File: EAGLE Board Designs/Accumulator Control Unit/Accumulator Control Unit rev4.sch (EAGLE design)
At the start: 240 parts, among them J1 CONNECTOR-2_MF_T_V_, J100 CONNECTOR-8_S_S, J2 CONNECTOR-8_MF_T_V_, J3 CONNECTOR-14_MF_T_V_, J4 JUMPER__1X02, J5 CONNECTOR-12_MF_T_V_, J6 CONNECTOR-CAN_μF_S_RA_, J7 CONNECTOR-2_MOLEX_NANOFIT_PTH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, Q1 TRANSISTOR_N_MOS__PMV15ENEA, Q100 TRANSISTOR_N_MOS__PMV15ENEA, Q101 TRANSISTOR_N_MOS__PMV15ENEA, Q2 TRANSISTOR_N_MOS__PMV15ENEA, T1 TRANSFORMER_HM2112ZNLT_AIRGAP, U1 RELAY_SOLIDSTATE_NO_DIP-4, U10 MAX7404, U100 ADG1423, U101 LM555, U11 OPAMP_1_CHANNEL_OPA991, U12 LOGICGATE_AND_DCK3, U13 OPAMP_1_CHANNEL_OPA991, U14 LOGICGATE_AND_DCK3, U15 OPAMP_1_CHANNEL_OPA991, U16 LOGICGATE_AND_DCK3, U17 OPAMP_1_CHANNEL_OPA991, U18 OPAMP_1_CHANNEL_OPA991, U19 MAX7404, U2 RELAY_SOLIDSTATE_NO_DIP-4, U20 OPAMP_1_CHANNEL_OPA991, U21 OPAMP_1_CHANNEL_OPA991, U22 OPAMP_1_CHANNEL_OPA991, U23 OPAMP_1_CHANNEL_OPA991, U24 OPAMP_1_CHANNEL_OPA991, U25 MAX7404, U26 VOLTAGE_REGULATOR_SOT-223_3.3V, U27 TCAN1051HQV-Q1, U28 OPAMP_1_CHANNEL_OPA991, U29 TCAN1051HQV-Q1, U3 OPAMP_1_CHANNEL_OPA991, U4 MAX7404, U5 LTC6820, U6 LOGICGATE_BUFFER, U7 ADM8316WBX30, U8 RELAY_SOLIDSTATE_NO_DIP-4, U9 OPAMP_1_CHANNEL_OPA991

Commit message: minor tweaks
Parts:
- added C46: CAPACITOR_0603_10V_0.1UF, HyTechDevices:CAPACITOR_0603_10V_0.1UF
- added J8: JUMPER__1X02, HyTechDevices:JUMPER__1X02
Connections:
- new net N$35: J8.2, R91.2
- net +3V3: now also C46.2, U29.VIO
- net CANH: no longer J6.CANH
- net CANL: no longer J6.CANL
- net EM_CANH: now also J6.CANH, J8.1, U29.CANH; no longer J3.3
- net EM_CANL: now also J6.CANL, R89.2, U29.CANL; no longer J3.2
- net GND: now also C46.1, U29.S
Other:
- moved on the sheet: C45, R26, R27, R89, R91

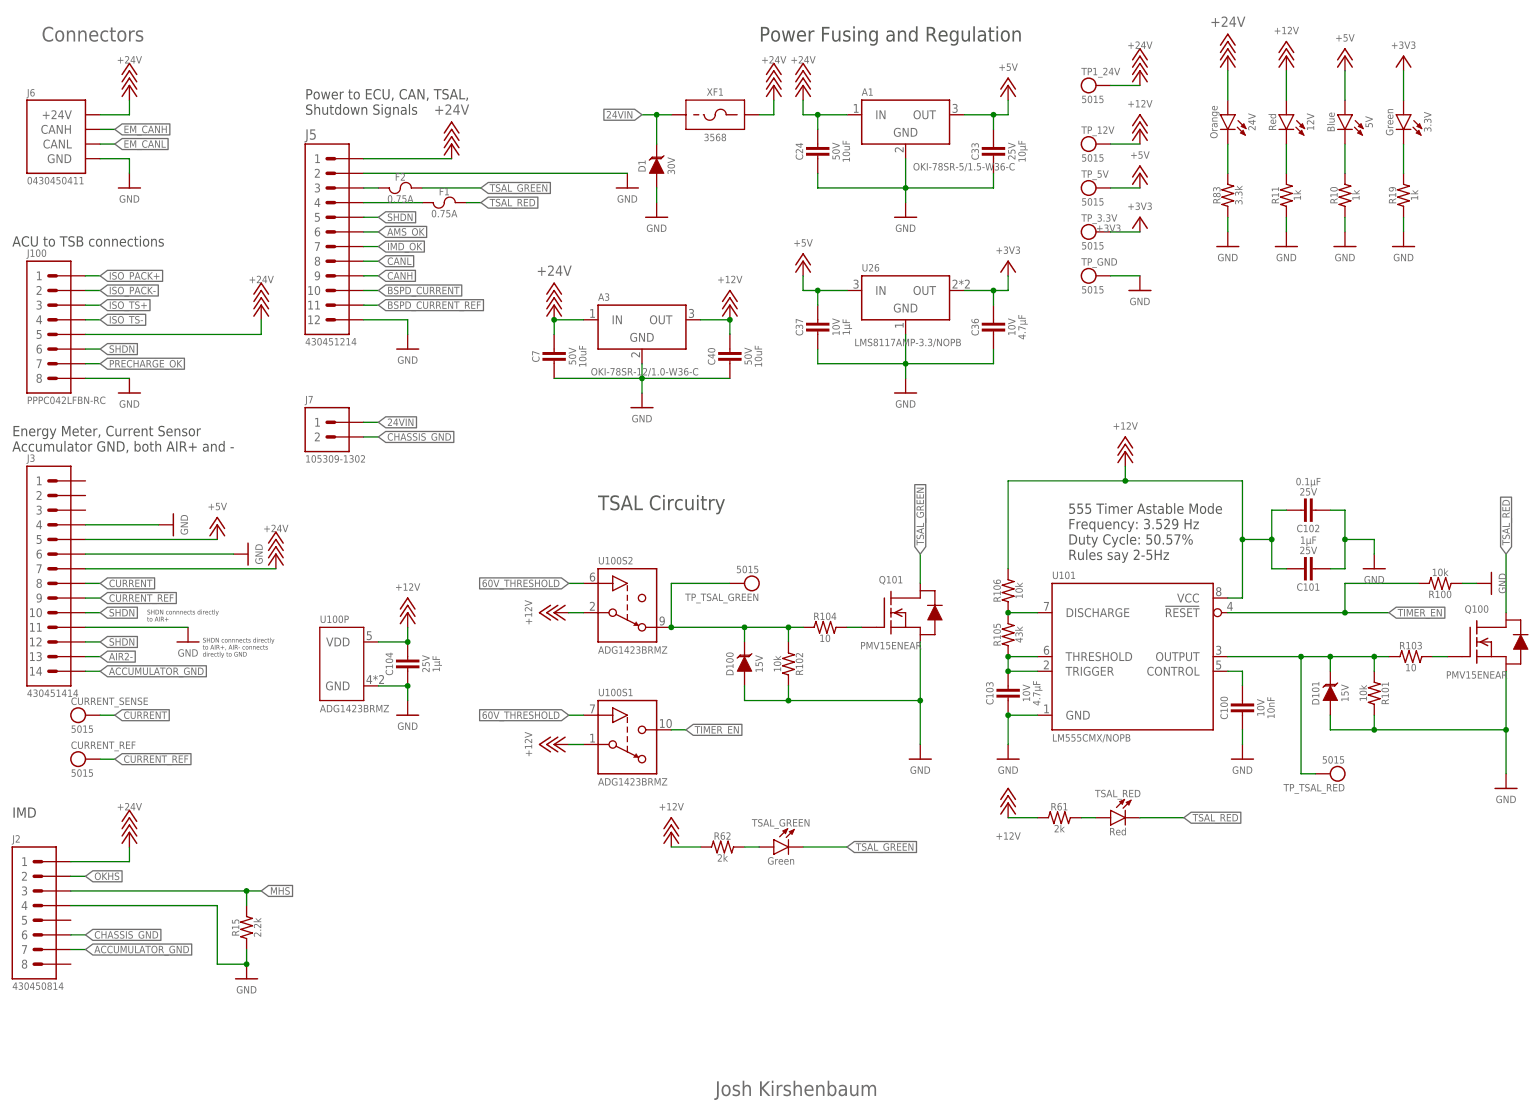
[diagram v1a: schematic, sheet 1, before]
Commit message: added inverter 24v switching
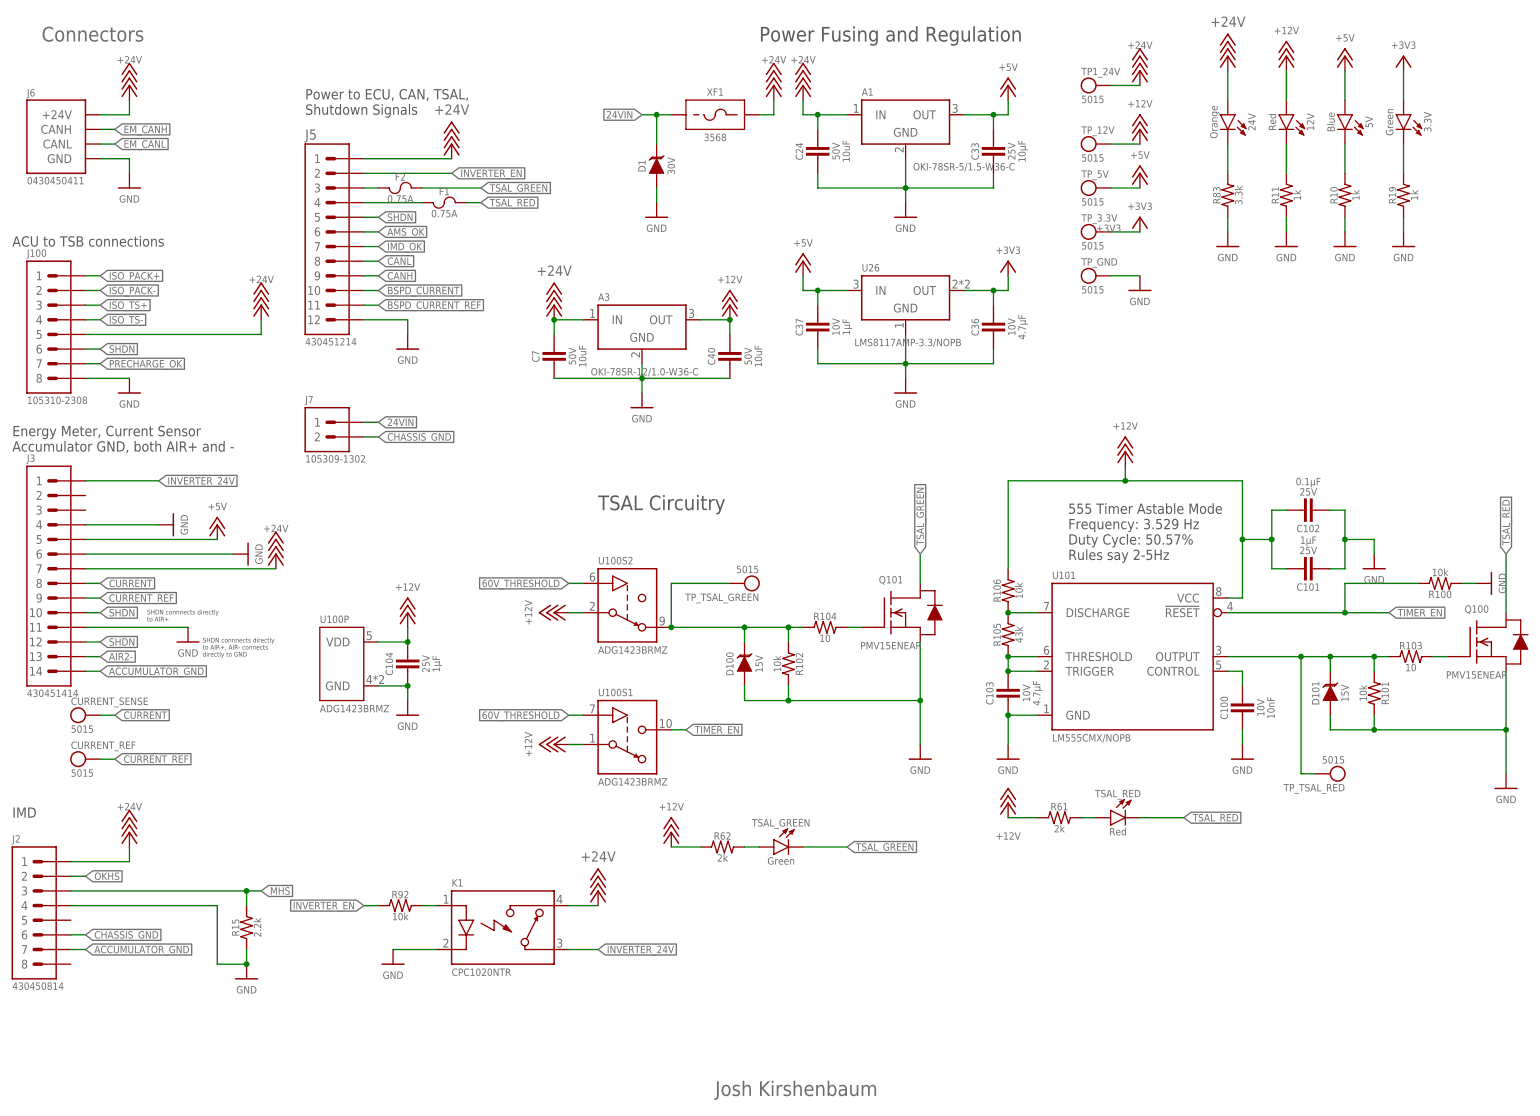
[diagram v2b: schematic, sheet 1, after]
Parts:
- added K1: RELAY_SOLIDSTATE_NO_CPC1020NTR, HyTechDevices:RELAY_SOLIDSTATE_NO_CPC1020NTR
- added R92: RESISTOR_0603_10K, HyTechDevices:RESISTOR_0603_10K
- J100: value CONNECTOR-8_S_S -> CONNECTOR-8_NF_T_V_NATURAL; device HyTechDevices:CONNECTOR-8_S_S -> HyTechDevices:CONNECTOR-8_NF_T_V_NATURAL
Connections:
- new net INVERTER_24V: J3.1, K1.CONTACT1
- new net INVERTER_EN: J5.2, R92.1
- new net N$38: K1.CONTROL+, R92.2
- net +24V: now also K1.CONTACT2
- net GND: now also K1.CONTROL-; no longer J5.2
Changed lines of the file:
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@@
 <part name="FRAME2" library="HyTechFrames" deviceset="FRAME" device=""/>
 <part name="FRAME4" library="HyTechFrames" deviceset="FRAME" device=""/>
-<part name="J100" library="HyTechDevices" deviceset="CONNECTOR-8_?_*" device="S" technology="S"/>
+<part name="J100" library="HyTechDevices" deviceset="CONNECTOR-8_?_*" device="NF_T_V" technology="NATURAL" value="CONNECTOR-8_NF_T_V_NATURAL"/>
 <part name="P1" library="HyTechSupplies" deviceset="+24V" device=""/>
 <part name="P2" library="HyTechSupplies" deviceset="GND" device=""/>
 <part name="P6" library="HyTechSupplies" deviceset="+24V" device=""/>
-<part name="P11" library="HyTechSupplies" deviceset="GND" device=""/>
 <part name="C24" library="HyTechDevices" deviceset="CAPACITOR_?_*" device="0805" technology="50V_10UF" value="CAPACITOR_0805_50V_10UF"/>
 <part name="C33" library="HyTechDevices" deviceset="CAPACITOR_?_*" device="0603" technology="25V_10UF"/>
@@
 <part name="P121" library="HyTechSupplies" deviceset="GND" device=""/>
 <part name="P122" library="HyTechSupplies" deviceset="GND" device=""/>
+<part name="K1" library="HyTechDevices" deviceset="RELAY_SOLIDSTATE_NO_*" device="CPC1020NTR"/>
+<part name="U$30" library="HyTechSupplies" deviceset="+24V" device=""/>
+<part name="P11" library="HyTechSupplies" deviceset="GND" device=""/>
+<part name="R92" library="HyTechDevices" deviceset="RESISTOR_?_*" device="0603" technology="10K"/>
 </parts>
 <sheets>
@@
 <attribute name="VALUE" x="50.8" y="163.83" size="1.27" layer="96" align="bottom-center"/>
 </instance>
-<instance part="P11" gate="1" x="114.3" y="180.34" smashed="yes">
-<attribute name="VALUE" x="114.3" y="179.07" size="1.27" layer="96" align="top-center"/>
-</instance>
 <instance part="C24" gate="G$1" x="147.32" y="187.96" smashed="yes" rot="R90">
 <attribute name="NAME" x="144.78" y="186.69" size="1.27" layer="95" rot="R90" align="bottom-center"/>
@@
 <instance part="P115" gate="1" x="76.2" y="152.4" smashed="yes">
 <attribute name="VALUE" x="76.2" y="151.13" size="1.27" layer="96" align="top-center"/>
+</instance>
+<instance part="K1" gate="G$1" x="83.82" y="58.42" smashed="yes">
+<attribute name="NAME" x="83.82" y="59.182" size="1.27" layer="95"/>
+<attribute name="MPN" x="83.82" y="44.958" size="1.27" layer="96" align="top-left"/>
+</instance>
+<instance part="U$30" gate="G$1" x="109.22" y="58.42" smashed="yes">
+<attribute name="VALUE" x="109.22" y="63.5" size="1.778" layer="96" align="bottom-center"/>
+</instance>
+<instance part="P11" gate="1" x="73.66" y="45.72" smashed="yes">
+<attribute name="VALUE" x="73.66" y="44.45" size="1.27" layer="96" align="top-center"/>
+</instance>
+<instance part="R92" gate="G$1" x="76.2" y="55.88" smashed="yes">
+<attribute name="NAME" x="74.93" y="57.15" size="1.27" layer="95" align="bottom-center"/>
+<attribute name="RESISTANCE" x="74.93" y="54.61" size="1.27" layer="96" align="top-center"/>
 </instance>
 </instances>
@@
 <wire x1="27.94" y1="185.42" x2="27.94" y2="182.88" width="0.1524" layer="91"/>
 <pinref part="J6" gate="G$1" pin="GND"/>
-</segment>
-<segment>
-<wire x1="68.58" y1="182.88" x2="114.3" y2="182.88" width="0.1524" layer="91"/>
-<pinref part="P11" gate="1" pin="GND"/>
-<pinref part="J5" gate="G$1" pin="2"/>
 </segment>
 <segment>
@@
 <wire x1="68.58" y1="157.48" x2="76.2" y2="157.48" width="0.1524" layer="91"/>
 <wire x1="76.2" y1="157.48" x2="76.2" y2="154.94" width="0.1524" layer="91"/>
+</segment>
+<segment>
+<pinref part="K1" gate="G$1" pin="CONTROL-"/>
+<wire x1="81.28" y1="48.26" x2="73.66" y2="48.26" width="0.1524" layer="91"/>
+<pinref part="P11" gate="1" pin="GND"/>
 </segment>
 </net>
@@
 <wire x1="68.58" y1="185.42" x2="83.82" y2="185.42" width="0.1524" layer="91"/>
 </segment>
+<segment>
+<pinref part="U$30" gate="G$1" pin="+24V"/>
+<pinref part="K1" gate="G$1" pin="CONTACT2"/>
+<wire x1="109.22" y1="55.88" x2="104.14" y2="55.88" width="0.1524" layer="91"/>
+</segment>
 </net>
 <net name="N$32" class="0">
@@
 </segment>
 </net>
+<net name="INVERTER_EN" class="0">
+<segment>
+<pinref part="J5" gate="G$1" pin="2"/>
+<wire x1="68.58" y1="182.88" x2="83.82" y2="182.88" width="0.1524" layer="91"/>
+<label x="83.82" y="182.88" size="1.27" layer="95" xref="yes"/>
+</segment>
+<segment>
+<wire x1="68.58" y1="55.88" x2="71.12" y2="55.88" width="0.1524" layer="91"/>
+<label x="68.58" y="55.88" size="1.27" layer="95" rot="R180" xref="yes"/>
+<pinref part="R92" gate="G$1" pin="1"/>
+</segment>
+</net>
+<net name="INVERTER_24V" class="0">
+<segment>
+<pinref part="J3" gate="G$1" pin="1"/>
+<wire x1="20.32" y1="129.54" x2="33.02" y2="129.54" width="0.1524" layer="91"/>
+<label x="33.02" y="129.54" size="1.27" layer="95" xref="yes"/>
+</segment>
+<segment>
+<pinref part="K1" gate="G$1" pin="CONTACT1"/>
+<wire x1="104.14" y1="48.26" x2="109.22" y2="48.26" width="0.1524" layer="91"/>
+<label x="109.22" y="48.26" size="1.27" layer="95" xref="yes"/>
+</segment>
+</net>
+<net name="N$38" class="0">
+<segment>
+<pinref part="K1" gate="G$1" pin="CONTROL+"/>
+<wire x1="81.28" y1="55.88" x2="78.74" y2="55.88" width="0.1524" layer="91"/>
+<pinref part="R92" gate="G$1" pin="2"/>
+</segment>
+</net>

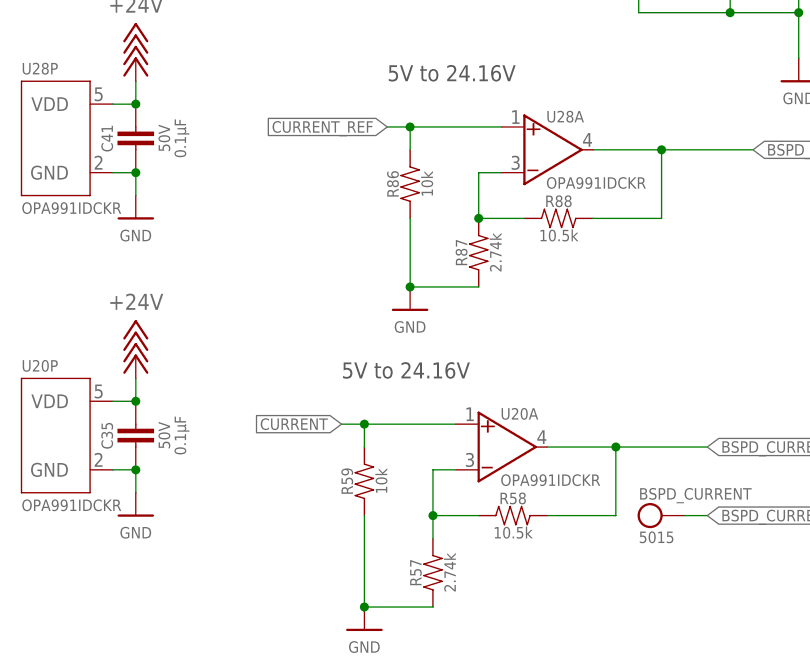
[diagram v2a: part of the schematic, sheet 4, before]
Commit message: changed pulldown resistors
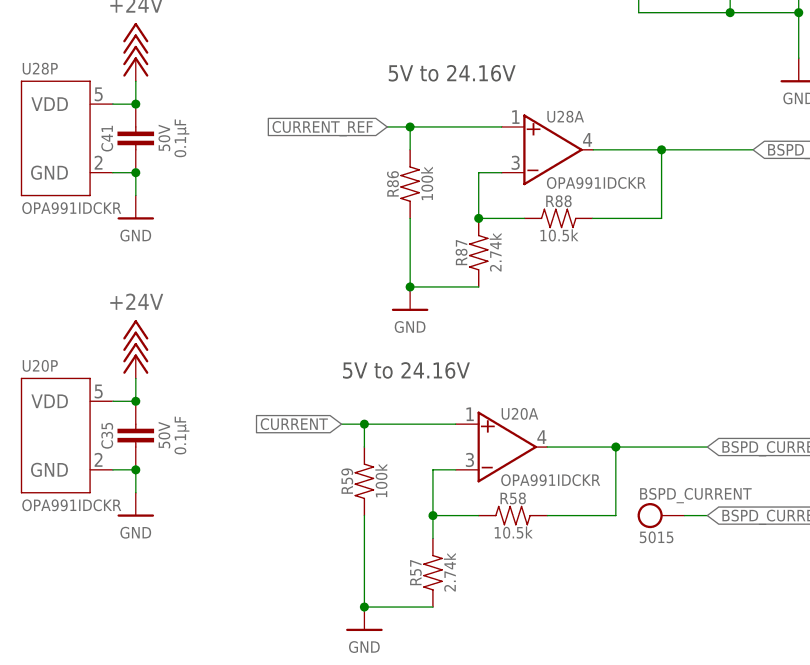
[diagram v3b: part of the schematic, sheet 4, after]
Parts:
- R59, R86: value RESISTOR_0603_10K -> RESISTOR_0603_100K; device HyTechDevices - Copy:RESISTOR_0603_10K -> HyTechDevices:RESISTOR_0603_100K
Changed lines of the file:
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@@
 <attribute name="REVIEWER_SCHEMATIC" value="Joshua Kirshenbaum"/>
 </part>
-<part name="R59" library="HyTechDevices - Copy" deviceset="RESISTOR_?_*" device="0603" technology="10K"/>
+<part name="R59" library="HyTechDevices" deviceset="RESISTOR_?_*" device="0603" technology="100K" value="RESISTOR_0603_100K"/>
 <part name="P39" library="HyTechSupplies" deviceset="GND" device=""/>
 <part name="R57" library="HyTechDevices" deviceset="RESISTOR_?_*" device="0603" technology="2.74K" value="RESISTOR_0603_2.74K"/>
@@
 <part name="P38" library="HyTechSupplies" deviceset="GND" device=""/>
 <part name="C41" library="HyTechDevices" deviceset="CAPACITOR_?_*" device="0603" technology="50V_0.1UF" value="CAPACITOR_0603_50V_0.1UF"/>
-<part name="R86" library="HyTechDevices - Copy" deviceset="RESISTOR_?_*" device="0603" technology="10K"/>
+<part name="R86" library="HyTechDevices" deviceset="RESISTOR_?_*" device="0603" technology="100K" value="RESISTOR_0603_100K"/>
 <part name="P70" library="HyTechSupplies" deviceset="GND" device=""/>
 <part name="R87" library="HyTechDevices" deviceset="RESISTOR_?_*" device="0603" technology="2.74K" value="RESISTOR_0603_2.74K"/>
